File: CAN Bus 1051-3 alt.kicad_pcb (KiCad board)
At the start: 2 copper layers, 14 x 14 mm, 14 parts, among them J1 Conn_01x05_Pin, J2 Conn_01x03_Pin, U1 TJA1051TK-3

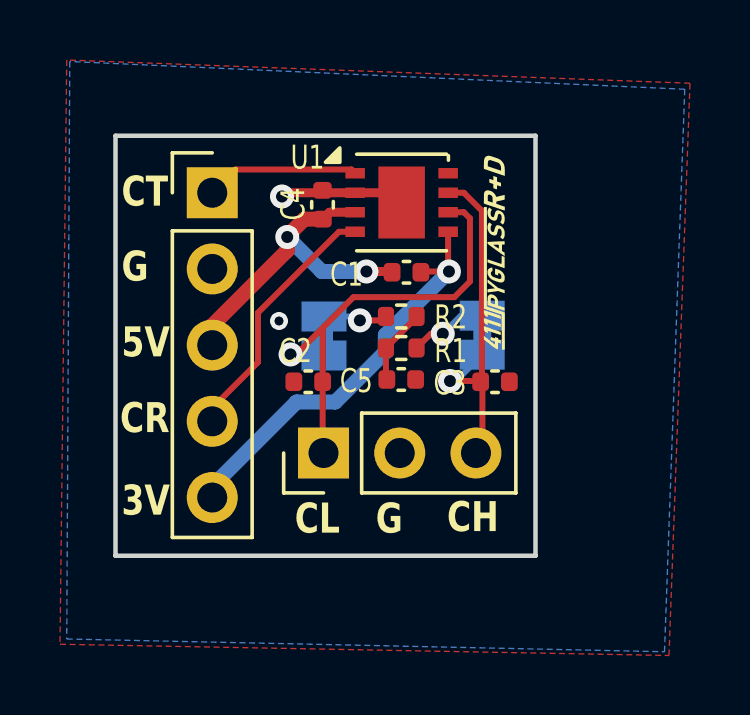
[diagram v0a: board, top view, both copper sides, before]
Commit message: alternate layout that conserves more space
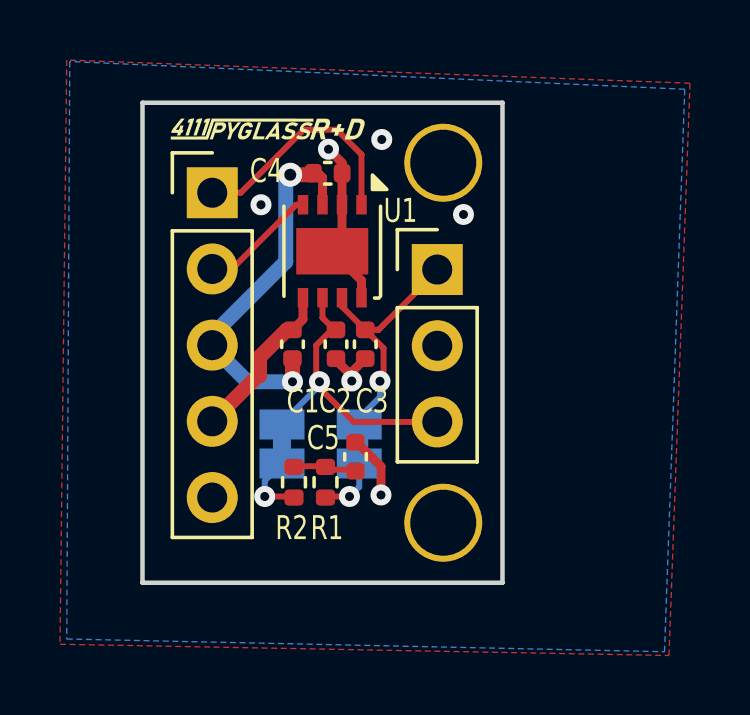
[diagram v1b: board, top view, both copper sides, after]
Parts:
- added H1: MountingHole, MountingHole:MountingHole_2.2mm_M2, F.Cu at (84.7, 85.5)
- added H2: MountingHole, MountingHole:MountingHole_2.2mm_M2, F.Cu at (84.7, 97.5)
- moved G*** 13.6 mm to (79.1, 99.5)
- moved G*** 8.81 mm to (79.0, 85.1), turned to 0 degrees
- moved J2 7.19 mm to (84.5, 89.0), turned to 0 degrees
- moved R2 6.58 mm to (79.8, 96.1), turned to -90 degrees
- moved JP1 5.47 mm to (81.9, 94.8), turned to 90 degrees
- moved R1 5.14 mm to (80.8, 96.1), turned to 90 degrees
- moved C3 4.50 mm to (82.1, 91.5), turned to -90 degrees
- moved C1 4.49 mm to (79.7, 91.5), turned to 90 degrees
- moved JP2 3.86 mm to (79.3, 94.8), turned to -90 degrees
- moved C5 2.99 mm to (81.8, 95.2), turned to -90 degrees
- moved U1 2.83 mm to (81.0, 88.4), turned to -90 degrees
- moved C2 1.56 mm to (81.2, 91.5), turned to -90 degrees
- moved C4 1.06 mm to (80.9, 85.8), turned to 0 degrees
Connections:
- J1 pad 2: GND -> /CAN_RX
- J1 pad 4: /CAN_RX -> +3V3
- J1 pad 5: +3V3 -> GND
- J2 pad 1: /CL -> /CH
- J2 pad 3: /CH -> /CL
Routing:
- net +3V3: track 13.8 -> 5.52 mm, vias 1 -> 0
- net /CL: track 16.1 -> 9.96 mm
- net GND: track 4.60 -> 9.32 mm, vias 2 -> 6
- net /CAN_RX: track 8.61 -> 3.91 mm
- net /CH: track 12.6 -> 8.42 mm
- net /CAN_TX: track 5.14 -> 8.50 mm
- net +4V: track 11.2 -> 13.4 mm
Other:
- board size 14 x 14 mm -> 12 x 16 mm
- board text added: "Term."
- board text removed: "Termintion"
